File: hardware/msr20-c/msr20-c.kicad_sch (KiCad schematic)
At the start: 0 parts

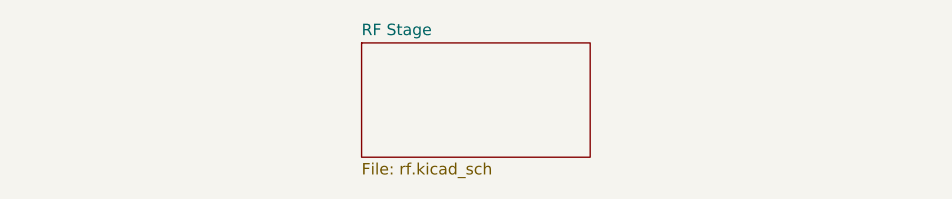
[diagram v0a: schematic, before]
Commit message: draft of rf stage
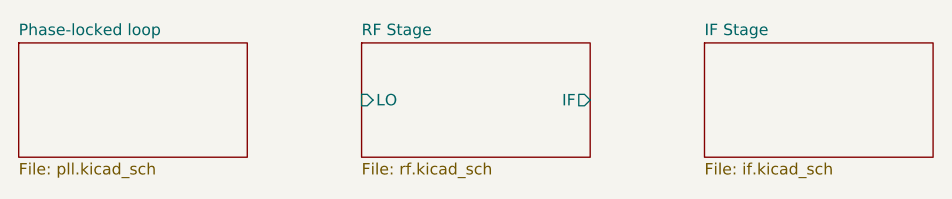
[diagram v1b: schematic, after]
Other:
- added sheet IF Stage (if.kicad_sch)
- added sheet Phase-locked loop (pll.kicad_sch)
- sheet RF Stage ports: added IF, LO; removed none
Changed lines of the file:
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@@
+	)
+	(sheet
+		(at 139.7 38.1)
+		(size 25.4 12.7)
+		(fields_autoplaced yes)
+		(stroke
+			(width 0.1524)
+			(type solid)
+		)
+		(fill
+			(color 0 0 0 0.0000)
+		)
+		(property "Sheetname" "IF Stage"
+			(at 139.7 37.3884 0)
+			(effects
+				(font
+					(size 1.27 1.27)
+				)
+				(justify left bottom)
+			)
+		)
+		(property "Sheetfile" "if.kicad_sch"
+			(at 139.7 51.3846 0)
+			(effects
+				(font
+					(size 1.27 1.27)
+				)
+				(justify left top)
+			)
+		)
+		(instances
+			(project "msr20-c"
+				(path "/3d24e86e-b070-4f0e-8c28-04e9dd9d95d1"
+					(page "3")
+				)
+			)
+		)
 	)
 	(sheet
@@
 			)
 		)
+		(pin "IF" output
+			(at 127 44.45 0)
+			(effects
+				(font
+					(size 1.27 1.27)
+				)
+				(justify right)
+			)
+		)
+		(pin "LO" input
+			(at 101.6 44.45 180)
+			(effects
+				(font
+					(size 1.27 1.27)
+				)
+				(justify left)
+			)
+		)
 		(instances
 			(project "msr20-c"
@@
 				)
 			)
+		)
+	)
+	(sheet
+		(at 63.5 38.1)
+		(size 25.4 12.7)
+		(fields_autoplaced yes)
+		(stroke
+			(width 0.1524)
+			(type solid)
+		)
+		(fill
+			(color 0 0 0 0.0000)
+		)
+		(property "Sheetname" "Phase-locked loop"
+			(at 63.5 37.3884 0)
+			(effects
+				(font
+					(size 1.27 1.27)
+				)
+				(justify left bottom)
+			)
+		)
+		(property "Sheetfile" "pll.kicad_sch"
+			(at 63.5 51.3846 0)
+			(effects
+				(font
+					(size 1.27 1.27)
+				)
+				(justify left top)
+			)
+		)
+		(instances
+			(project "msr20-c"
+				(path "/3d24e86e-b070-4f0e-8c28-04e9dd9d95d1"
+					(page "4")
+				)
+			)

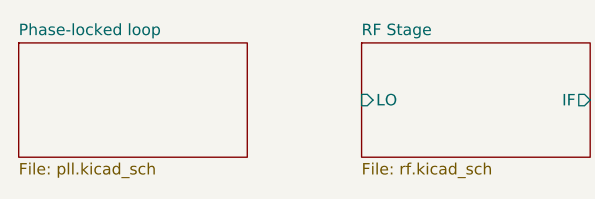
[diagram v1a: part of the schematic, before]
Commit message: add pll to schematic
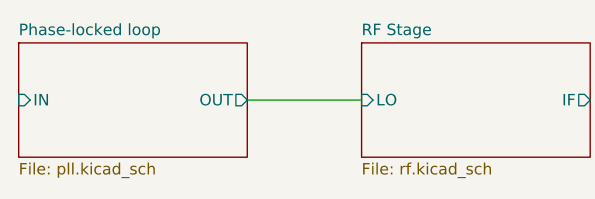
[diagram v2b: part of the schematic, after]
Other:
- sheet Phase-locked loop ports: added IN, OUT; removed none
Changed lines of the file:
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@@
 		(rev "1")
+	)
+	(wire
+		(pts
+			(xy 88.9 44.45) (xy 101.6 44.45)
+		)
+		(stroke
+			(width 0)
+			(type default)
+		)
 	)
 	(sheet
@@
 			)
 		)
+		(pin "IN" input
+			(at 63.5 44.45 180)
+			(effects
+				(font
+					(size 1.27 1.27)
+				)
+				(justify left)
+			)
+		)
+		(pin "OUT" output
+			(at 88.9 44.45 0)
+			(effects
+				(font
+					(size 1.27 1.27)
+				)
+				(justify right)
+			)
+		)

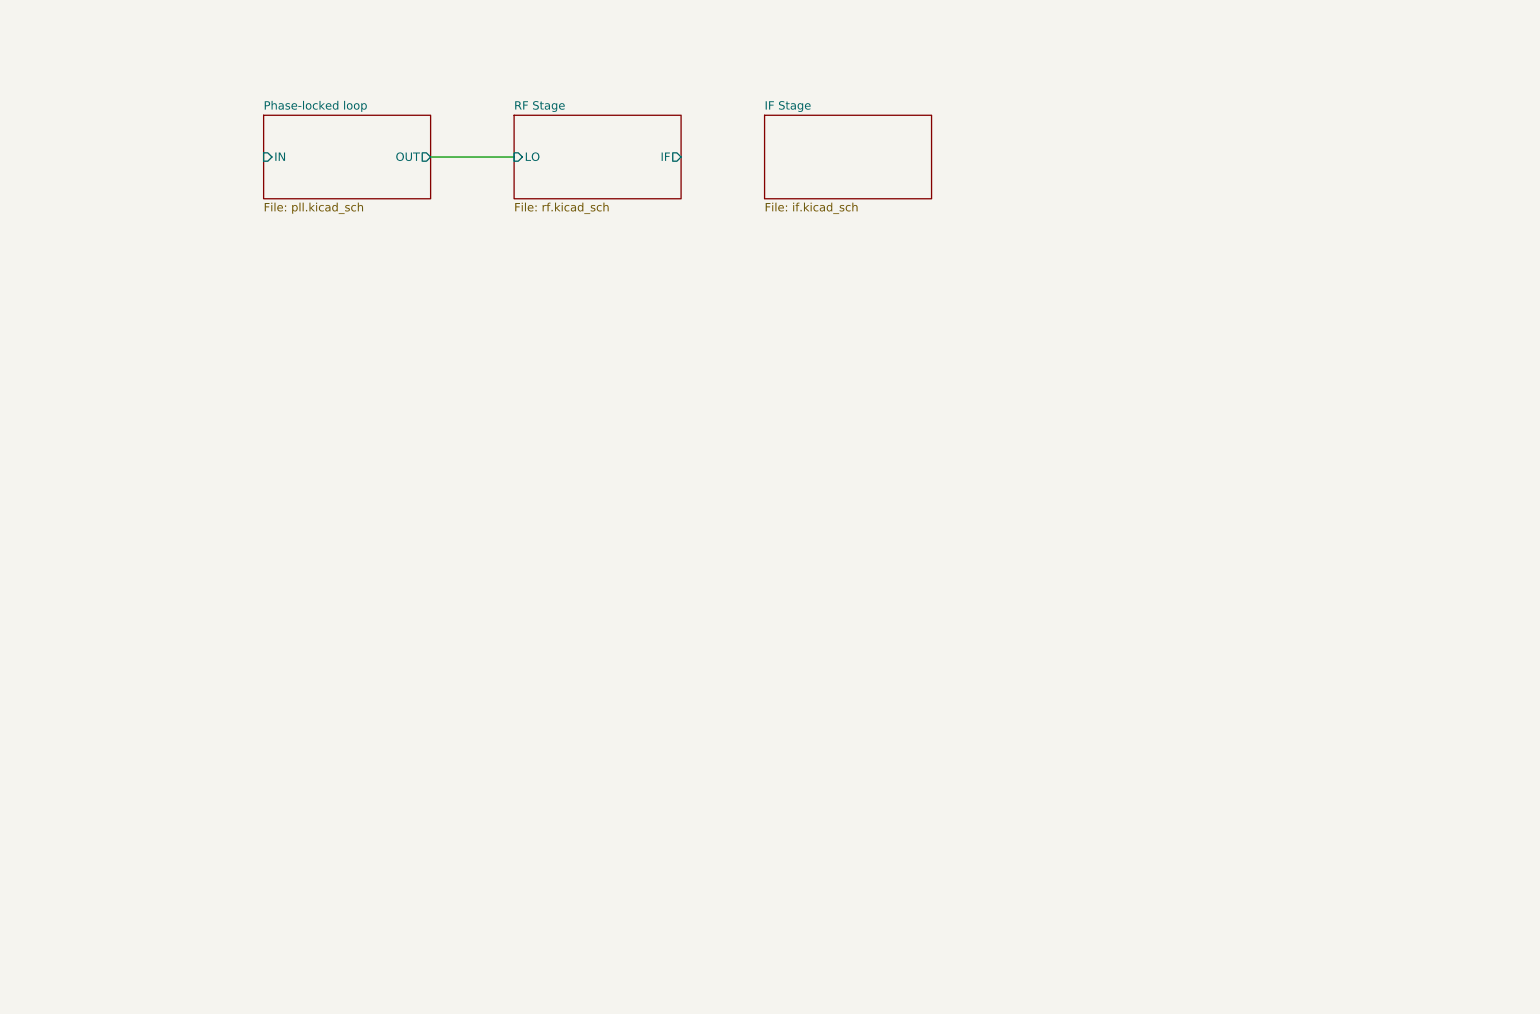
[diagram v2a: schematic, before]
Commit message: add pico to schematic
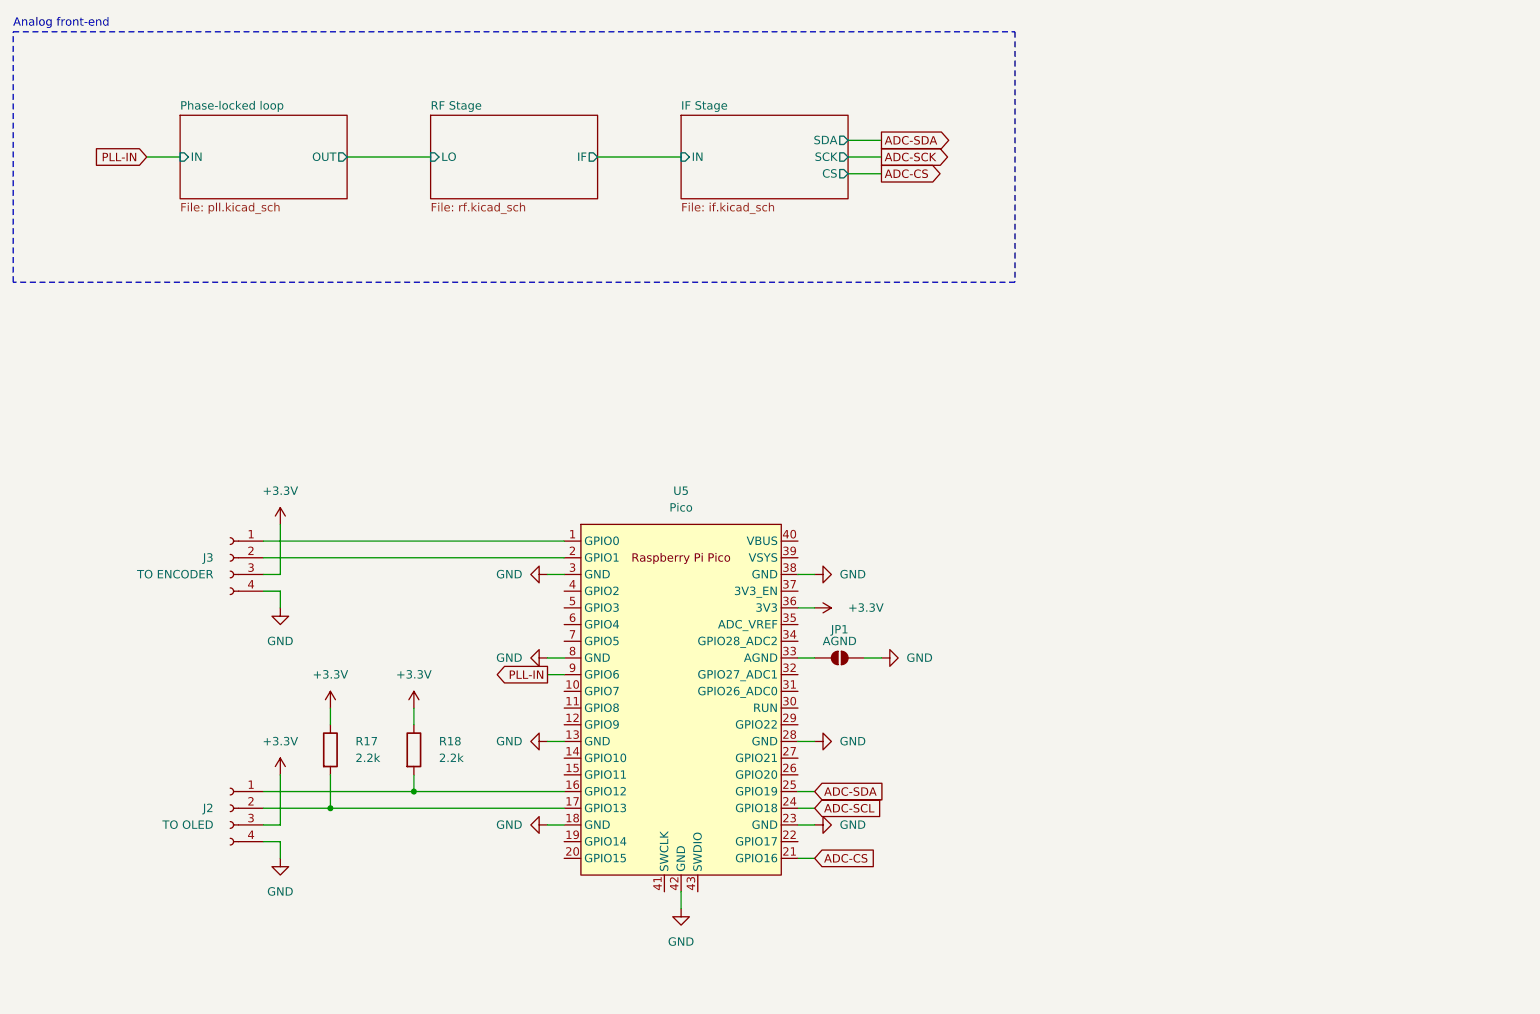
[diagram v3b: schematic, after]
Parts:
- added J2: TO OLED, symbol Connector:Conn_01x04_Socket
- added J3: TO ENCODER, symbol Connector:Conn_01x04_Socket
- added JP1: AGND, symbol Jumper:SolderJumper_2_Open
- added R17, R18: 2.2k, symbol Device:R
- added U5: Pico, RPi_Pico:RPi_Pico_SMD_TH, symbol MCU_RaspberryPi_and_Boards:Pico
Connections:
- new net: J3.1 (Pin_1), U5.1 (GPIO0)
- new net: J3.2 (Pin_2), U5.2 (GPIO1)
- new net: J2.1 (Pin_1), R18.2, U5.16 (GPIO12)
- new net: J2.2 (Pin_2), R17.2, U5.17 (GPIO13)
- new net: JP1.1 (A), U5.33 (AGND)
- new net +3.3V: J2.3 (Pin_3), J3.3 (Pin_3), R17.1, R18.1, U5.36 (3V3)
- new net ADC-CS: U5.21 (GPIO16)
- new net ADC-SCL: U5.24 (GPIO18)
- new net ADC-SDA: U5.25 (GPIO19)
- new net GND: J2.4 (Pin_4), J3.4 (Pin_4), JP1.2 (B), U5.13 (GND), U5.18 (GND), U5.23 (GND), U5.28 (GND), U5.3 (GND), U5.38 (GND), U5.42 (GND), U5.8 (GND)
- new net PLL-IN: U5.9 (GPIO6)
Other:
- sheet IF Stage ports: added CS, IN, SCK, SDA; removed none
- note added: "Analog front-end"

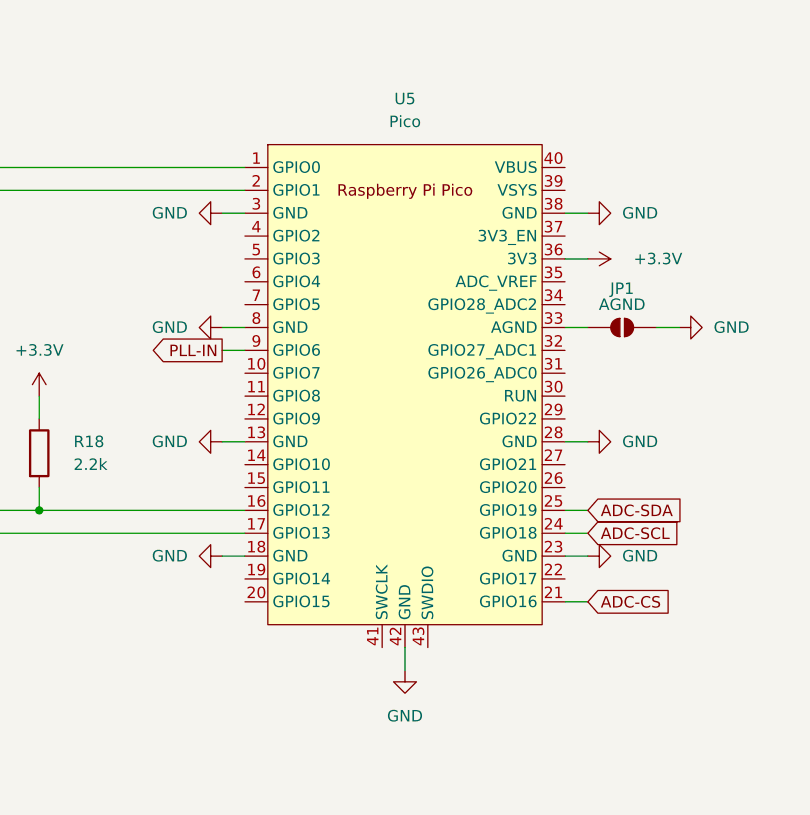
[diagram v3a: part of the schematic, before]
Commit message: add swd connector to schematic
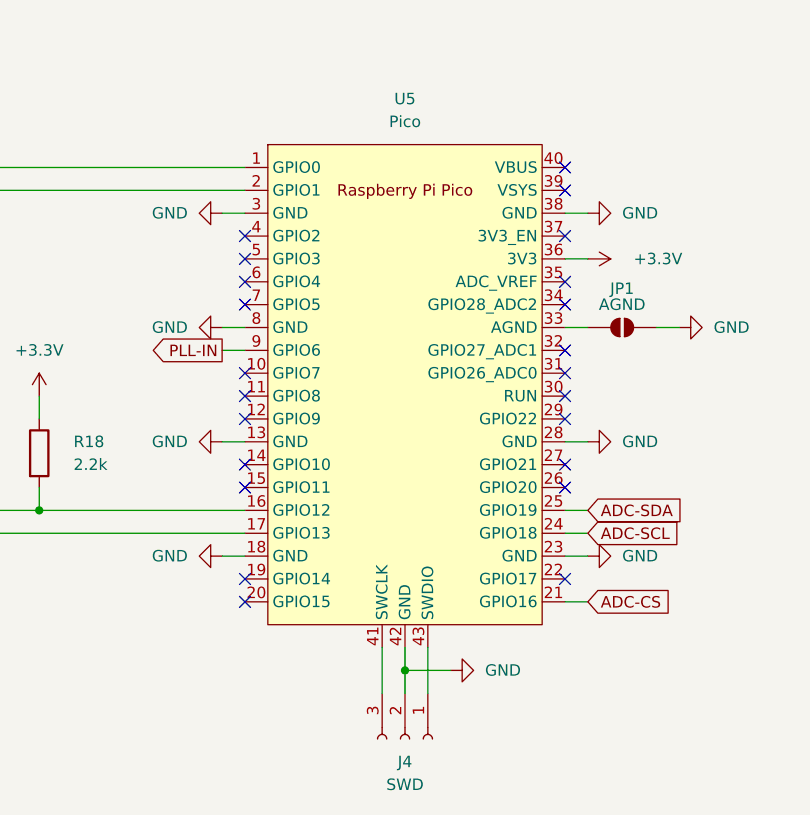
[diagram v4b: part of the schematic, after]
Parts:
- added J4: SWD, symbol Connector:Conn_01x03_Socket
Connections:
- net GND: now also J4.2 (Pin_2)
- net at U5.41 (SWCLK): now also J4.3 (Pin_3)
- net at U5.43 (SWDIO): now also J4.1 (Pin_1)
- no-connect marks 0 -> 23
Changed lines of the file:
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@@
+	)
+	(junction
+		(at 127 158.75)
+		(diameter 0)
+		(color 0 0 0 0)
 	)
 	(junction
@@
 		(color 0 0 0 0)
 	)
+	(no_connect
+		(at 144.78 115.57)
+	)
+	(no_connect
+		(at 109.22 113.03)
+	)
+	(no_connect
+		(at 109.22 118.11)
+	)
+	(no_connect
+		(at 109.22 148.59)
+	)
+	(no_connect
+		(at 109.22 110.49)
+	)
+	(no_connect
+		(at 144.78 123.19)
+	)
+	(no_connect
+		(at 144.78 105.41)
+	)
+	(no_connect
+		(at 109.22 115.57)
+	)
+	(no_connect
+		(at 109.22 138.43)
+	)
+	(no_connect
+		(at 109.22 135.89)
+	)
+	(no_connect
+		(at 109.22 130.81)
+	)
+	(no_connect
+		(at 144.78 135.89)
+	)
+	(no_connect
+		(at 144.78 125.73)
+	)
+	(no_connect
+		(at 144.78 110.49)
+	)
+	(no_connect
+		(at 109.22 128.27)
+	)
+	(no_connect
+		(at 109.22 125.73)
+	)
+	(no_connect
+		(at 144.78 148.59)
+	)
+	(no_connect
+		(at 144.78 128.27)
+	)
+	(no_connect
+		(at 144.78 118.11)
+	)
+	(no_connect
+		(at 144.78 130.81)
+	)
+	(no_connect
+		(at 144.78 138.43)
+	)
+	(no_connect
+		(at 144.78 102.87)
+	)
+	(no_connect
+		(at 109.22 151.13)
+	)
 	(wire
 		(pts
@@
 	(wire
 		(pts
+			(xy 127 156.21) (xy 127 158.75)
+		)
+		(stroke
+			(width 0)
+			(type default)
+		)
+	)
+	(wire
+		(pts
 			(xy 86.36 138.43) (xy 86.36 140.97)
 		)
@@
 	(wire
 		(pts
-			(xy 127 156.21) (xy 127 158.75)
-		)
-		(stroke
-			(width 0)
-			(type default)
-		)
-	)
-	(wire
-		(pts
 			(xy 73.66 128.27) (xy 73.66 130.81)
 		)
@@
 	(wire
 		(pts
+			(xy 127 158.75) (xy 127 161.29)
+		)
+		(stroke
+			(width 0)
+			(type default)
+		)
+	)
+	(wire
+		(pts
 			(xy 45.72 44.45) (xy 50.8 44.45)
 		)
@@
 	(wire
 		(pts
+			(xy 129.54 156.21) (xy 129.54 161.29)
+		)
+		(stroke
+			(width 0)
+			(type default)
+		)
+	)
+	(wire
+		(pts
 			(xy 66.04 107.95) (xy 66.04 100.33)
 		)
@@
 	(wire
 		(pts
+			(xy 127 158.75) (xy 132.08 158.75)
+		)
+		(stroke
+			(width 0)
+			(type default)
+		)
+	)
+	(wire
+		(pts
 			(xy 63.5 110.49) (xy 66.04 110.49)
 		)
@@
 		(pts
 			(xy 63.5 107.95) (xy 66.04 107.95)
+		)
+		(stroke
+			(width 0)
+			(type default)
+		)
+	)
+	(wire
+		(pts
+			(xy 124.46 156.21) (xy 124.46 161.29)
 		)
 		(stroke
@@
 	(symbol
 		(lib_id "power:GND")
-		(at 127 158.75 0)
-		(unit 1)
-		(exclude_from_sim no)
-		(in_bom yes)
-		(on_board yes)
-		(dnp no)
-		(fields_autoplaced yes)
-		(property "Reference" "#PWR044"
-			(at 127 165.1 0)
-			(effects
-				(font
-					(size 1.27 1.27)
-				)
-				(hide yes)
-			)
-		)
-		(property "Value" "GND"
-			(at 127 163.83 0)
-			(effects
-				(font
-					(size 1.27 1.27)
-				)
-			)
-		)
-		(property "Footprint" ""
-			(at 127 158.75 0)
-			(effects
-				(font
-					(size 1.27 1.27)
-				)
-				(hide yes)
-			)
-		)
-		(property "Datasheet" ""
-			(at 127 158.75 0)
-			(effects
-				(font
-					(size 1.27 1.27)
-				)
-				(hide yes)
-			)
-		)
-		(property "Description" "Power symbol creates a global label with name \"GND\" , ground"
-			(at 127 158.75 0)
-			(effects
-				(font
-					(size 1.27 1.27)
-				)
-				(hide yes)
-			)
-		)
-		(pin "1"
-		)
-		(instances
-			(project "msr20-c"
-				(path "/3d24e86e-b070-4f0e-8c28-04e9dd9d95d1"
-					(reference "#PWR044")
-					(unit 1)
-				)
-			)
-		)
-	)
-	(symbol
-		(lib_id "power:GND")
 		(at 106.68 107.95 270)
 		(unit 1)
@@
 					(unit 1)
 				)
+			)
+		)
+	)
+	(symbol
+		(lib_id "Connector:Conn_01x03_Socket")
+		(at 127 166.37 270)
+		(unit 1)
+		(exclude_from_sim no)
+		(in_bom yes)
+		(on_board yes)
+		(dnp no)
+		(fields_autoplaced yes)
+		(property "Reference" "J4"
+			(at 127 168.91 90)
+			(effects
+				(font
+					(size 1.27 1.27)
+				)
+			)
+		)
+		(property "Value" "SWD"
+			(at 127 171.45 90)
+			(effects
+				(font
+					(size 1.27 1.27)
+				)
+			)
+		)
+		(property "Footprint" ""
+			(at 127 166.37 0)
+			(effects
+				(font
+					(size 1.27 1.27)
+				)
+				(hide yes)
+			)
+		)
+		(property "Datasheet" "~"
+			(at 127 166.37 0)
+			(effects
+				(font
+					(size 1.27 1.27)
+				)
+				(hide yes)
+			)
+		)
+		(property "Description" "Generic connector, single row, 01x03, script generated"
+			(at 127 166.37 0)
+			(effects
+				(font
+					(size 1.27 1.27)
+				)
+				(hide yes)
+			)
+		)
+		(pin "1"
+		)
+		(pin "3"
+		)
+		(pin "2"
+		)
+		(instances
+			(project "msr20-c"
+				(path "/3d24e86e-b070-4f0e-8c28-04e9dd9d95d1"
+					(reference "J4")
+					(unit 1)
+				)
+			)
+		)
+	)
+	(symbol
+		(lib_id "power:GND")
+		(at 132.08 158.75 90)
+		(unit 1)
+		(exclude_from_sim no)
+		(in_bom yes)
+		(on_board yes)
+		(dnp no)
+		(fields_autoplaced yes)
+		(property "Reference" "#PWR044"
+			(at 138.43 158.75 0)
+			(effects
+				(font
+					(size 1.27 1.27)
+				)
+				(hide yes)
+			)
+		)
+		(property "Value" "GND"
+			(at 135.89 158.7499 90)
+			(effects
+				(font
+					(size 1.27 1.27)
+				)
+				(justify right)
+			)
+		)
+		(property "Footprint" ""
+			(at 132.08 158.75 0)
+			(effects
+				(font
+					(size 1.27 1.27)
+				)
+				(hide yes)
+			)
+		)
+		(property "Datasheet" ""
+			(at 132.08 158.75 0)
+			(effects
+				(font
+					(size 1.27 1.27)
+				)
+				(hide yes)
+			)
+		)
+		(property "Description" "Power symbol creates a global label with name \"GND\" , ground"
+			(at 132.08 158.75 0)
+			(effects
+				(font
+					(size 1.27 1.27)
+				)
+				(hide yes)
+			)
+		)
+		(pin "1"
+		)
+		(instances
+			(project "msr20-c"
+				(path "/3d24e86e-b070-4f0e-8c28-04e9dd9d95d1"
+					(reference "#PWR044")
+					(unit 1)
+				)

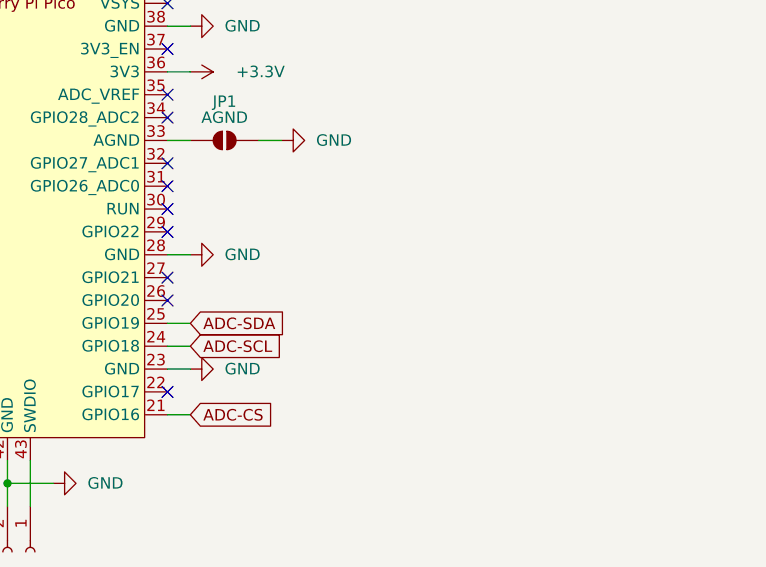
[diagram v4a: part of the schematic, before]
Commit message: add audio out and lpf to sch
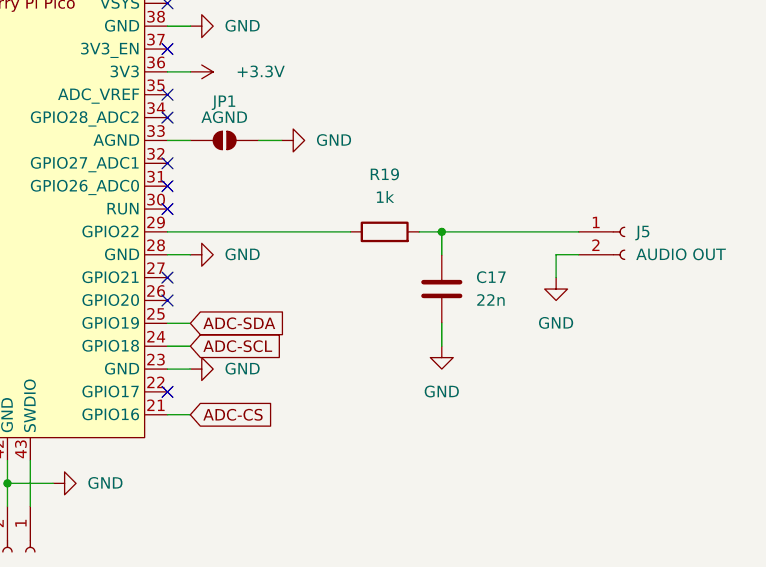
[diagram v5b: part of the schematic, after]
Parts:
- added C17: 22n, symbol Device:C
- added J5: AUDIO OUT, symbol Connector:Conn_01x02_Socket
- added R19: 1k, symbol Device:R
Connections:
- net GND: now also C17.2, J5.2 (Pin_2)
- net at U5.29 (GPIO22): now also R19.1
- new net: C17.1, J5.1 (Pin_1), R19.2
- no-connect marks 23 -> 22
